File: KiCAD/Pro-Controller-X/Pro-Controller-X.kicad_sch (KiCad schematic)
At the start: 12 parts, among them U1 TP4056

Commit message: PCB Started
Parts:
- added Q1: 2N7002, Package_TO_SOT_SMD:SOT-23, symbol Transistor_FET:2N7002
- added U2: ~, ProControllerX:Wii U Outline, symbol ProControllerX:ProController
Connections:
- net GND: now also U2.21, U2.22, U2.23, U2.24, U2.25, U2.26, U2.27, U2.28, U2.29, U2.30, U2.31, U2.32, U2.33, U2.34, U2.35, U2.36, U2.37, U2.38, U2.42 (Gnd)

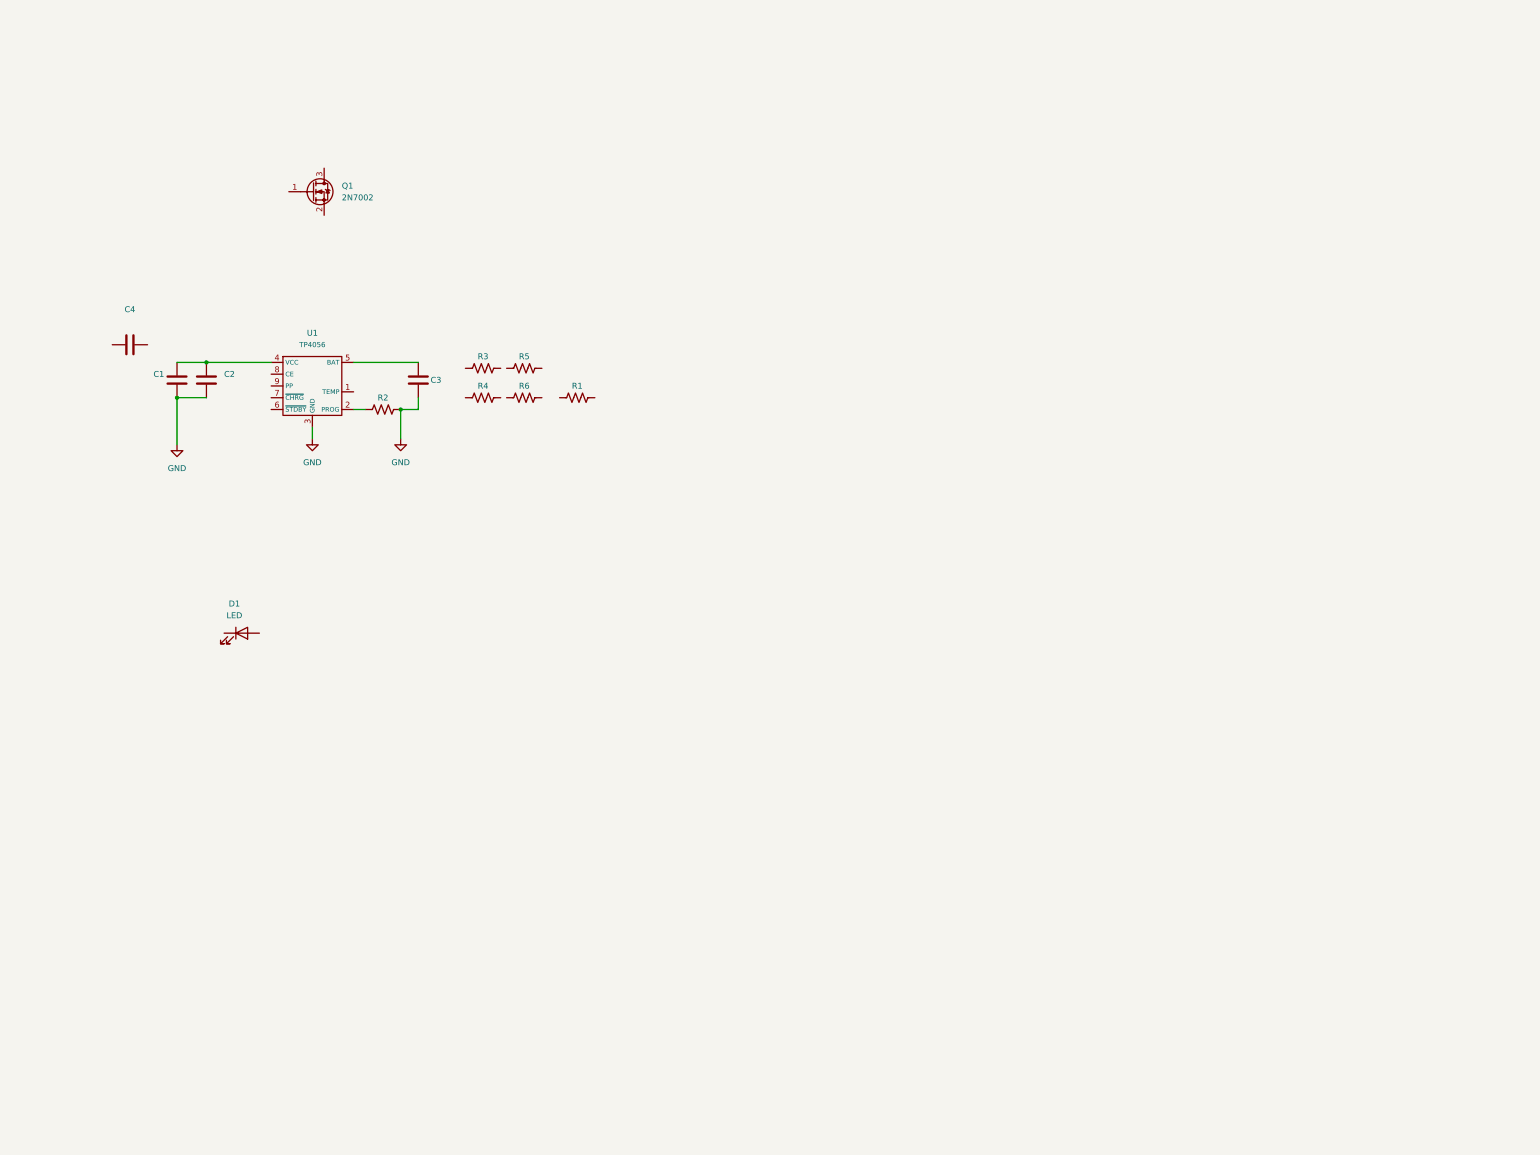
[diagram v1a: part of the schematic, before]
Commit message: Top Center Schematics Mapped - parts not accurate
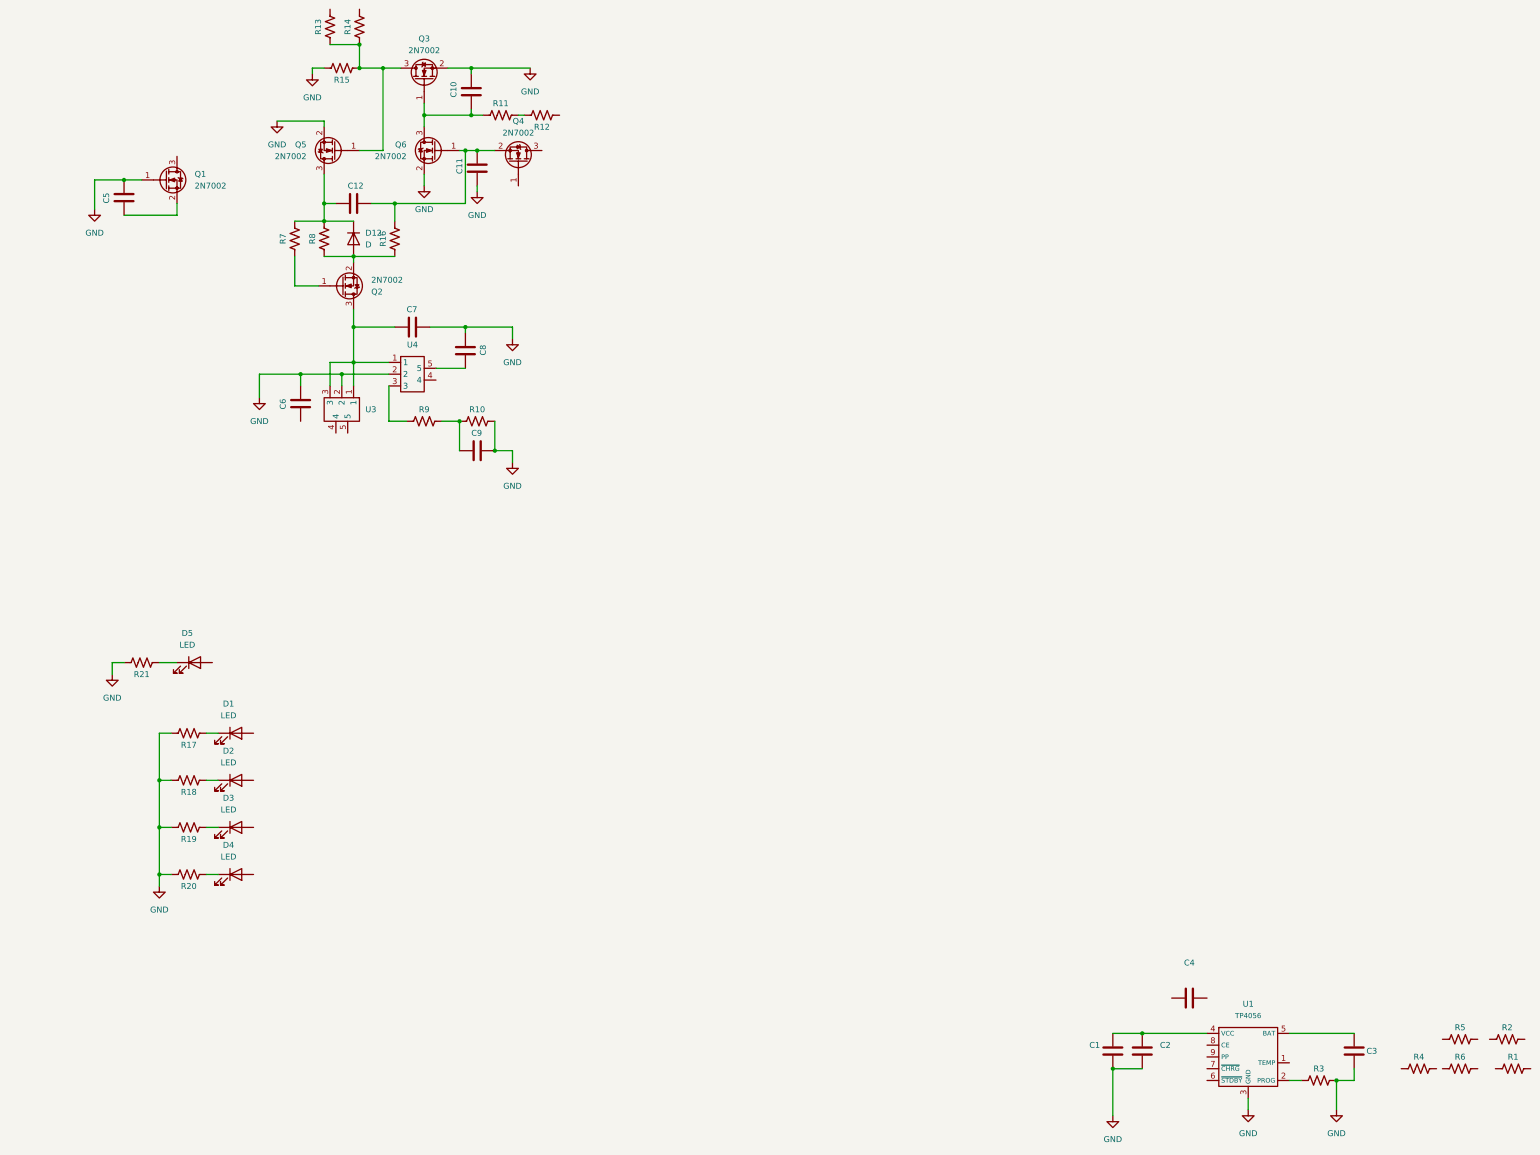
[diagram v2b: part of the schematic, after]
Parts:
- added C10, C11, C12, C5, C6, C7, C8: C, Capacitor_SMD:C_0805_2012Metric_Pad1.18x1.45mm_HandSolder, symbol Device:C
- added C9: C, Capacitor_SMD:C_0603_1608Metric, symbol Device:C
- added D12: D, Capacitor_SMD:C_0805_2012Metric, symbol Device:D
- added D2, D3, D4, D5: LED, symbol Device:LED
- added Q2, Q4, Q5: 2N7002, Package_TO_SOT_SMD:SuperSOT-3, symbol Transistor_FET:2N7002
- added Q3, Q6: 2N7002, Package_TO_SOT_SMD:SOT-23, symbol Transistor_FET:2N7002
- added R10, R11, R12, R13, R14, R15, R16, R17, R18, R19, R20, R21, R7, R8, R9: R_US, Resistor_SMD:R_0402_1005Metric_Pad0.72x0.64mm_HandSolder, symbol Device:R_US
- added U3, U4: ~, Package_TO_SOT_SMD:SOT-23-5, symbol ProControllerX:SOT-23_5-Blank
- C1, C3: footprint (none) -> Capacitor_SMD:C_0805_2012Metric_Pad1.18x1.45mm_HandSolder
- C2, C4: footprint (none) -> Capacitor_SMD:C_0402_1005Metric_Pad0.74x0.62mm_HandSolder
- R1, R2, R3, R4, R5, R6: footprint (none) -> Resistor_SMD:R_0402_1005Metric_Pad0.72x0.64mm_HandSolder
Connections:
- net GND: now also Q1.1 (G), R3.2, C10.2, C11.1, C5.2, C6.2, C7.2, C8.1, C9.2, Q3.2 (S), Q5.2 (S), Q6.2 (S), R10.2, R15.2, R17.2, R18.2, R19.2, R20.2, R21.2, U3.2, U4.2; no longer R2.2
- net at R3.1: now also U1.2 (PROG)
- net at D1.1 (K): now also R17.1
- net at R2.1: no longer U1.2 (PROG)
- net at Q1.2 (S): now also C5.1
- new net: C7.1, Q2.3 (D), U3.1, U3.3, U4.1
- new net: R9.1, U4.3
- new net: C8.2, U4.5
- new net: D12.2 (A), Q2.2 (S), R16.1, R8.1
- new net: C11.2, C12.2, Q4.2 (S), Q6.1 (G), R16.2
- new net: D4.1 (K), R20.1
- new net: D5.1 (K), R21.1
- new net: C10.1, Q3.1 (G), Q6.3 (D), R11.1
- new net: Q3.3 (D), Q5.1 (G), R13.1, R14.1, R15.1
- new net: D3.1 (K), R19.1
- new net: R11.2, R12.2
- new net: C9.1, R10.1, R9.2
- new net: D2.1 (K), R18.1
- new net: C12.1, D12.1 (K), Q5.3 (D), R7.2, R8.2
- new net: Q2.1 (G), R7.1
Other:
- moved on the sheet: C1, C2, C3, C4, D1, Q1, R1, R3, R4, R5, R6, U1

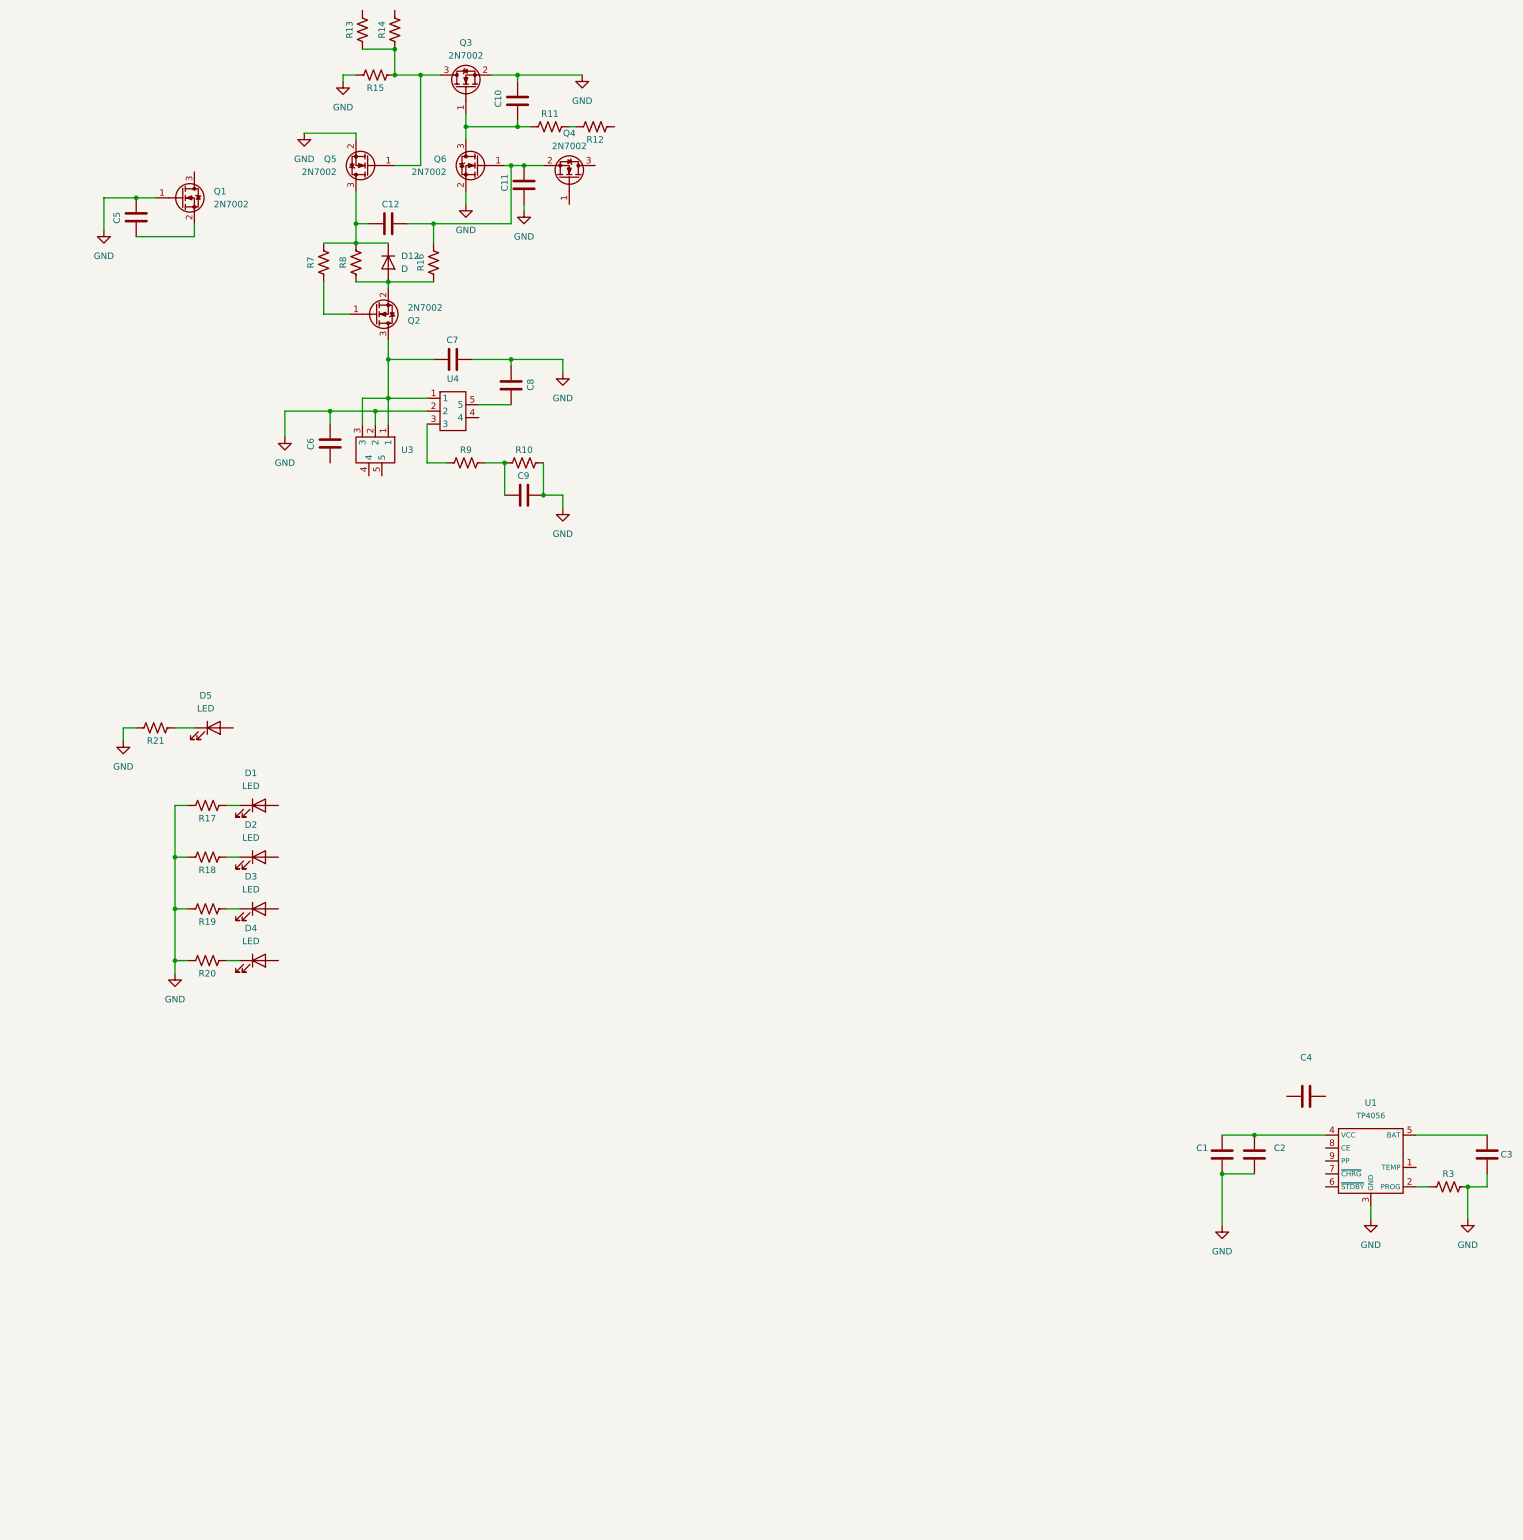
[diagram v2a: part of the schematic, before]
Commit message: Most components implemented and roughly grouped
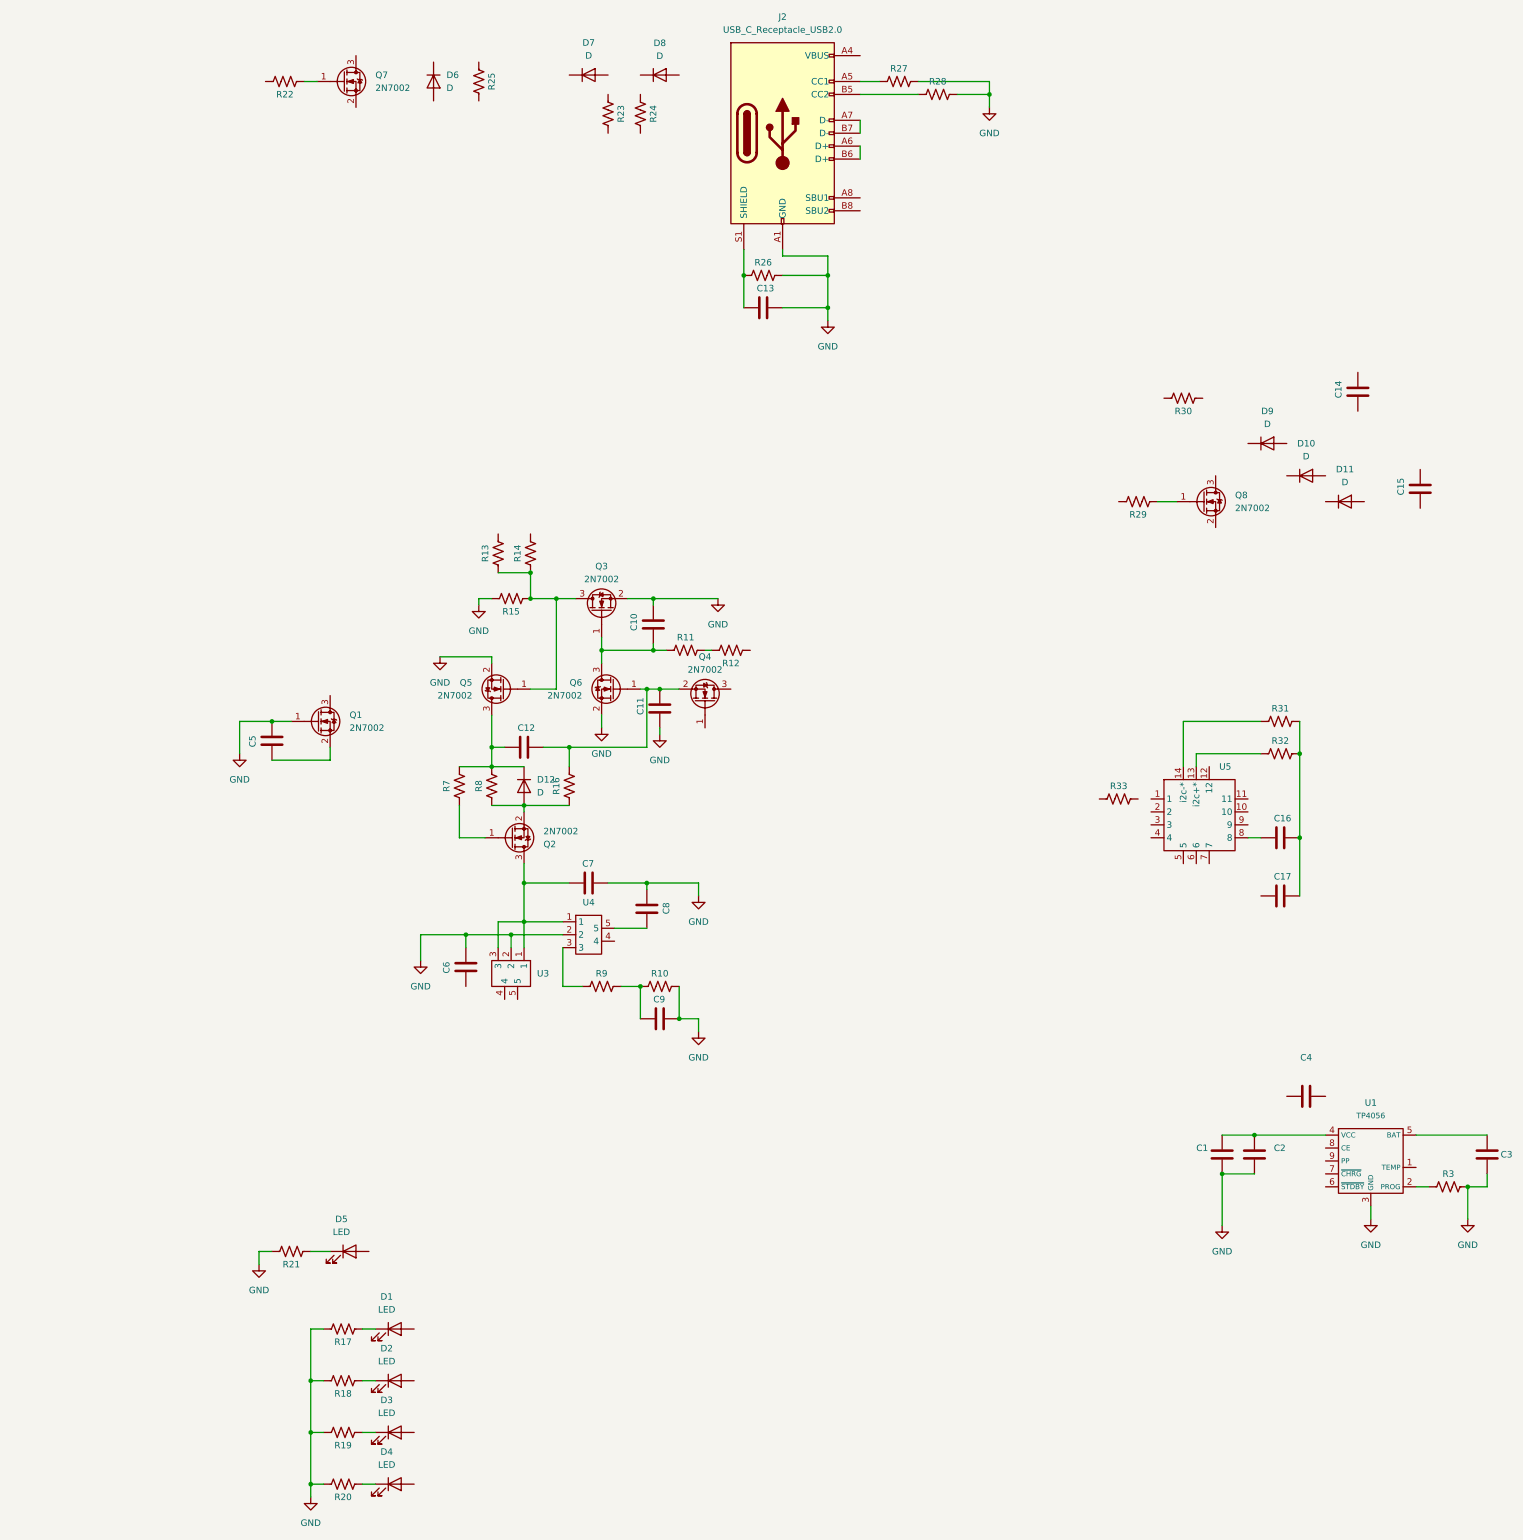
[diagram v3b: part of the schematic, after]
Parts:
- added C13, C16, C17: C, Capacitor_SMD:C_0603_1608Metric, symbol Device:C
- added C14, C15: C, Capacitor_SMD:C_0805_2012Metric_Pad1.18x1.45mm_HandSolder, symbol Device:C
- added D10, D11, D6, D7, D8, D9: D, Capacitor_SMD:C_0805_2012Metric, symbol Device:D
- added J2: USB_C_Receptacle_USB2.0, Connector_USB:USB_C_Receptacle_GCT_USB4085, symbol Connector:USB_C_Receptacle_USB2.0
- added Q7, Q8: 2N7002, Package_TO_SOT_SMD:SOT-23, symbol Transistor_FET:2N7002
- added R22, R23, R24, R25, R26, R27, R28, R29, R31, R32, R33: R_US, Resistor_SMD:R_0402_1005Metric_Pad0.72x0.64mm_HandSolder, symbol Device:R_US
- added R30: R_US, Resistor_SMD:R_0805_2012Metric, symbol Device:R_US
- added U5: ~, Package_LGA:LGA-14_3x2.5mm_P0.5mm_LayoutBorder3x4y, symbol ProControllerX:Gyro
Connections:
- net GND: now also C13.2, J2.A1 (GND), J2.A12 (GND), J2.B1 (GND), J2.B12 (GND), R26.2, R27.2, R28.2
- new net: R32.1, U5.13 (i2c+*)
- new net: R31.1, U5.14 (i2c-*)
- new net: C16.1, U5.8
- new net: J2.A4 (VBUS), J2.A9 (VBUS), J2.B4 (VBUS), J2.B9 (VBUS)
- new net: J2.A5 (CC1), R27.1
- new net: J2.A6 (D+), J2.B6 (D+)
- new net: J2.A7 (D-), J2.B7 (D-)
- new net: J2.B5 (CC2), R28.1
- new net: C13.1, J2.S1 (SHIELD), R26.1
- new net: C16.2, C17.2, R31.2, R32.2
- new net: Q8.1 (G), R29.1
- new net: Q7.1 (G), R22.1
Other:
- moved on the sheet: C10, C11, C12, C5, C6, C7, C8, C9, D1, D12, D2, D3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

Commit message: Started Mapping Traces
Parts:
- added D13: D, Capacitor_SMD:C_0805_2012Metric, symbol Device:D
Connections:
- net GND: now also C14.2, C15.1, C4.1, D11.2 (A), D6.2 (A), D7.1 (K), D8.2 (A), D9.1 (K), Q8.2 (S), R2.1, R25.2, R5.2, U1.9 (PP), D13.2 (A)
- net at D8.1 (K): now also J2.A7 (D-), J2.B7 (D-), R24.1
- net at J2.A4 (VBUS), J2.A9 (VBUS), J2.B4 (VBUS)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: now also D6.1 (K), Q7.3 (D), R25.1
- net at J2.A6 (D+), J2.B6 (D+): now also D7.2 (A), R23.1
- net VDD: now reaches D12.2 (A), Q2.2 (S), R16.1, R8.1
- net VDD: now also C3.1, U1.5 (BAT), D13.1 (K)
- net VCC: now reaches Q7.2 (S)
- net VCC: now also C1.2, C2.2, R1.2, R4.1, U1.4 (VCC), U1.8 (CE)
- net RDIV-BC: now reaches R1.1
- net RDIV-BC: now also C4.2, R2.2
- net at C14.1: now also D10.1 (K), D9.2 (A), R30.1
- net at C15.2: now also D10.2 (A), D11.1 (K)
- net at R4.2: now also R5.1, R6.1, U1.1 (TEMP)
- net at Q8.3 (D): now also R30.2
- net CHRG: now reaches U1.7 (~{CHRG})
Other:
- moved on the sheet: C14, C15, C4, D10, D11, D6, D7, D8, D9, Q7, Q8, R1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
